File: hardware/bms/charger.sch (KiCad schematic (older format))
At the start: 1 part

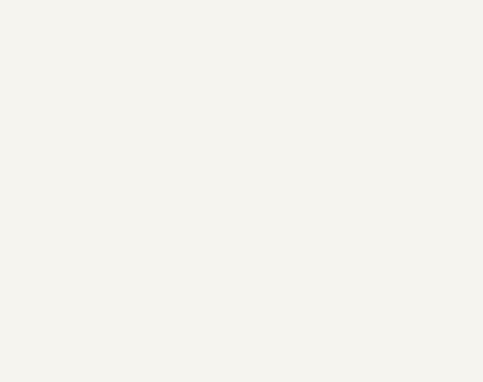
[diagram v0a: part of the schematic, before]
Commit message: Battery monitor / balancer schematic complete. Charger is next. Thinking of adding MCU directly to this board if layout space allows, probably doesn't deserve its own board (or just deserves a dev board)
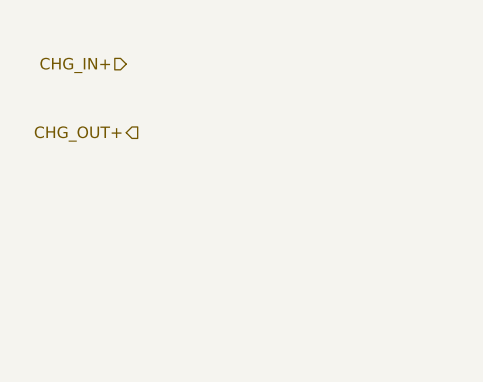
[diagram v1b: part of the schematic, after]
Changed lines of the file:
@@
 $Descr A4 11693 8268
 encoding utf-8
-Sheet 4 5
+Sheet 3 4
 Title ""
 Date ""
@@
 	1    0    0    -1
 $EndComp
+Text HLabel 3300 2600 0    50   Input ~ 0
+CHG_IN+
+Text HLabel 3350 2900 0    50   Output ~ 0
+CHG_OUT+
 $EndSCHEMATC
